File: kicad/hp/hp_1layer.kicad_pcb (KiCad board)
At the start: 2 copper layers, 42 x 30 mm, 15 parts, among them J1 FROM AMP L-G-R, J2 SPK L, J3 SPK R, J4 3.5mm TRS, J5 PANEL JACK T-G-R, SW1 SPK / HP

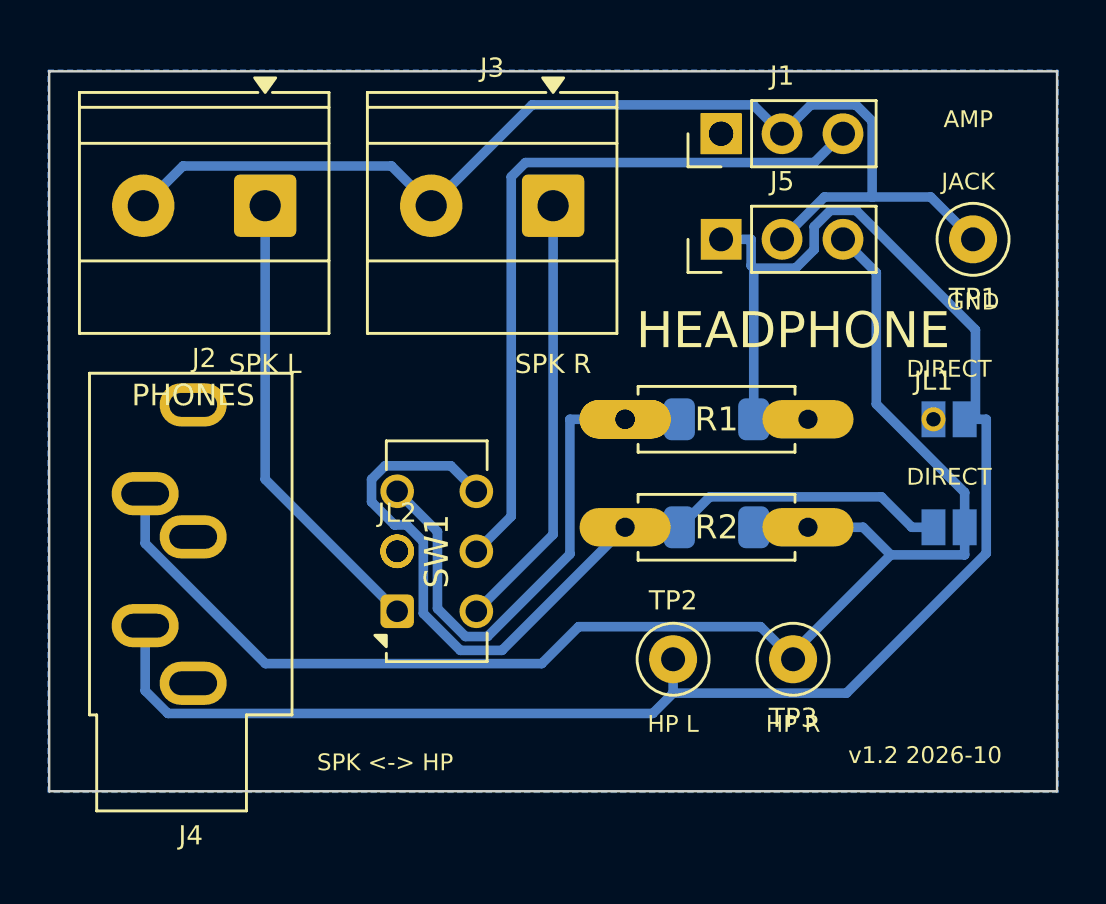
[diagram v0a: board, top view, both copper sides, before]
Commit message: Headphone jack sleeve pad was left without its GND net
pcbgen stripped the SMD-twin suffix from every pad number ending in S, which turned the jack's
sleeve pad "S" into an empty key. Exact pad numbers are matched first now. Headphone boards,
panel, images and the release zip rebuilt; single-layer headphone board 3 wire links, clean.
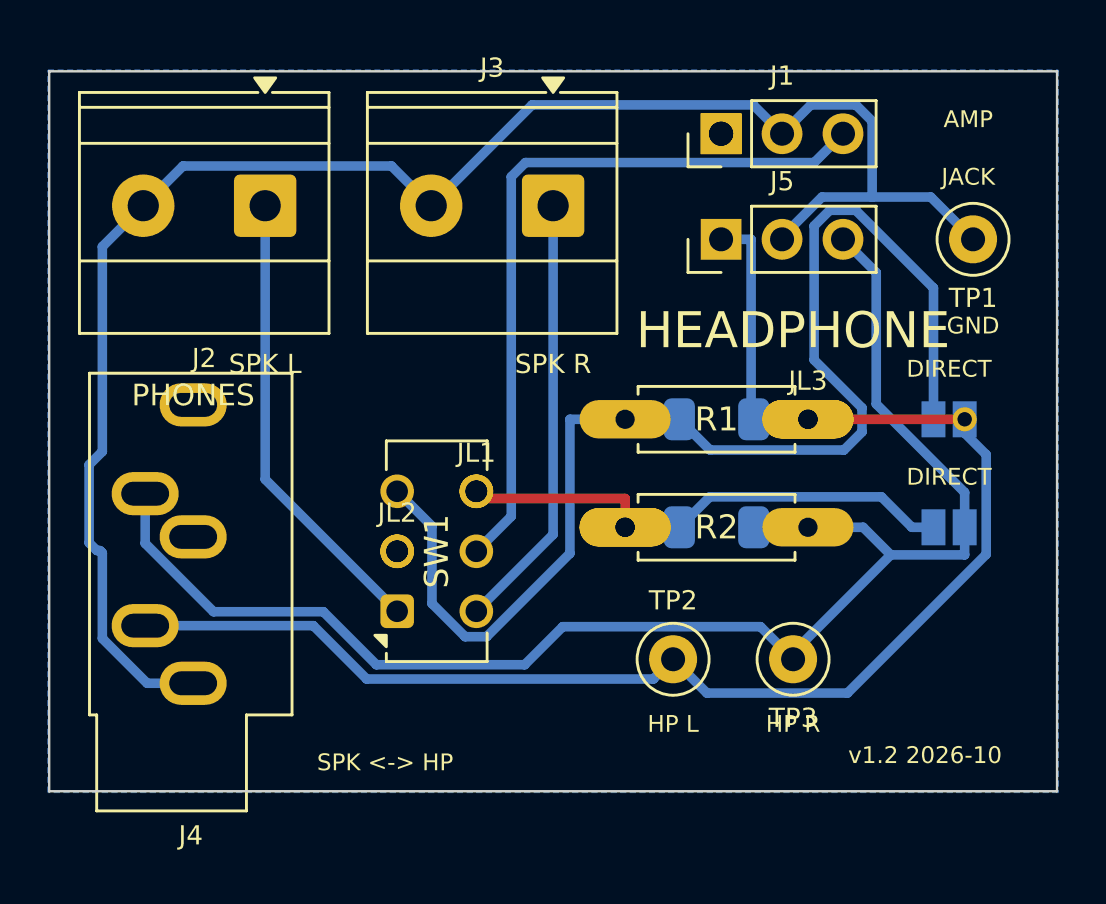
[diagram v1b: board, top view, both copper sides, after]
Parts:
- added JL3: wire link, Custom:WireLink, F.Cu at (81.6, 64.5)
- moved JL1 19.3 mm to (67.8, 67.5)
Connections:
- J4 pad S: (no net) -> GND
- JL1 pad 1: /HP_L -> /HP_R
- JL1 pad 2: /HP_L -> /HP_R
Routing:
- net /HP_L: track 23.2 -> 53.1 mm
- net GND: track 47.3 -> 71.2 mm
- net /HP_R: track 36.9 -> 21.4 mm
- net /JACK_L: track 76.5 -> 62.9 mm
